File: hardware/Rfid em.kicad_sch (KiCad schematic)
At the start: 21 parts, among them IC1 EM4095, J1 Conn_01x06, U1 560uH, U2 AMS1117-5.0

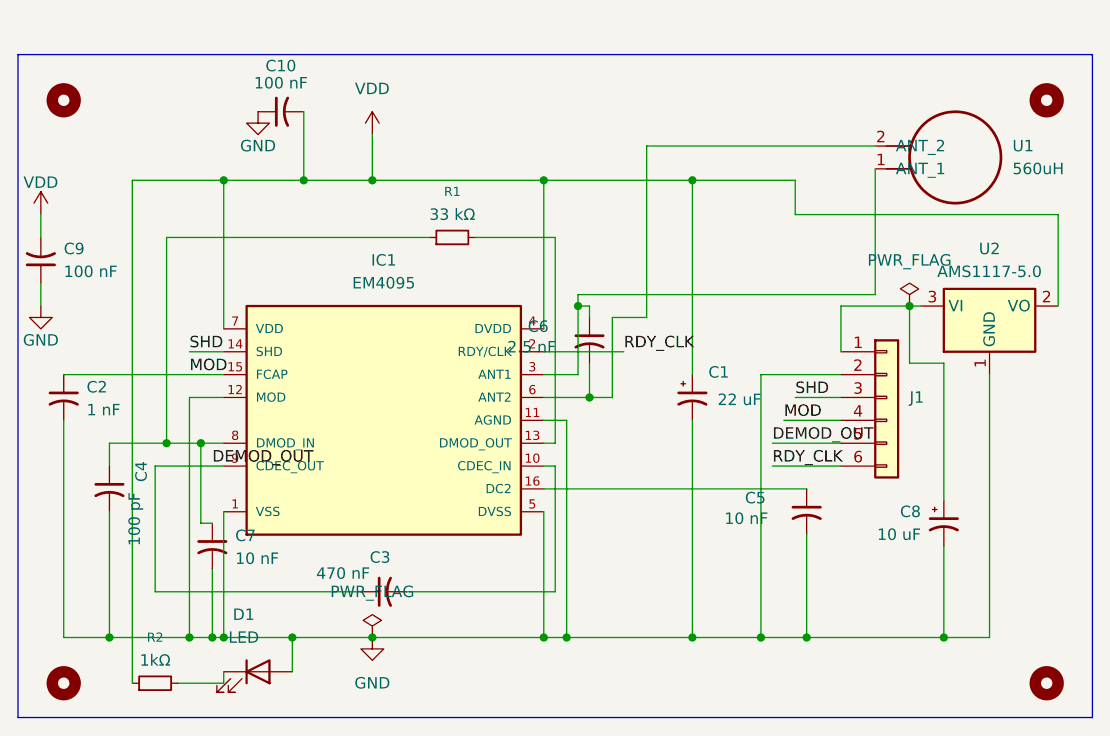
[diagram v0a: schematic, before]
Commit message: fix: Wire EM4095 per datasheet Fig. 8 and tune antenna to 134.2 kHz
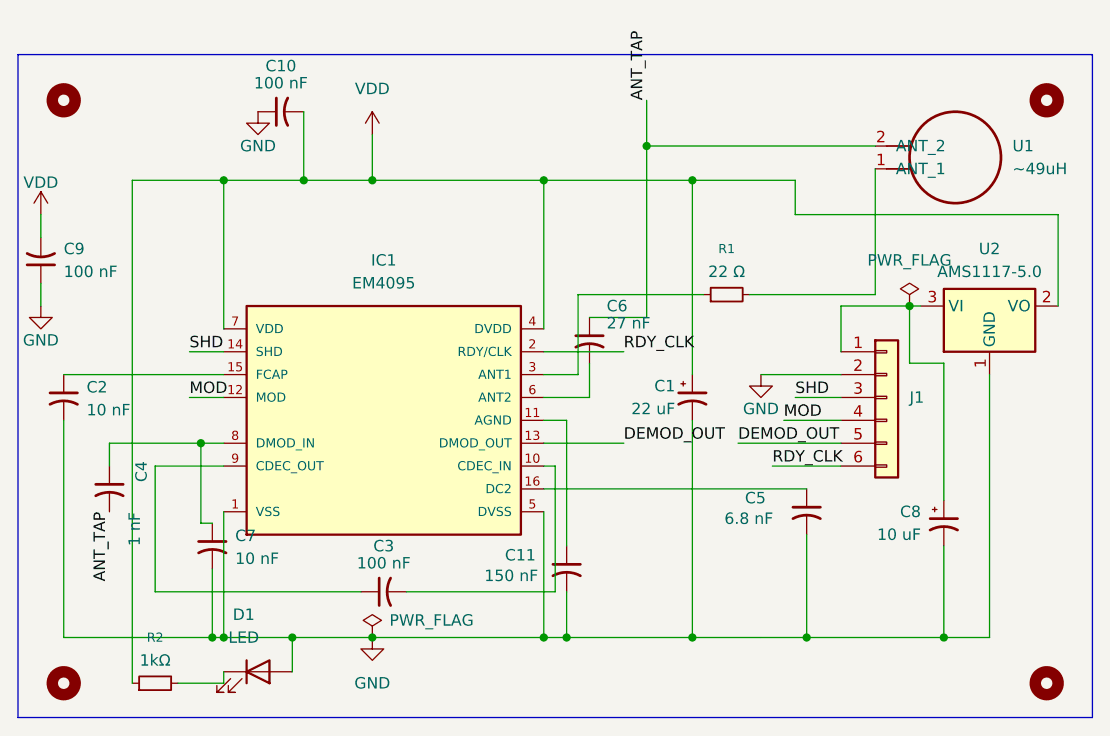
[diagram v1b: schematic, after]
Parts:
- added C11: 150 nF, Capacitor_SMD:C_0805_2012Metric, symbol Device:C_Small_US
- C2: value 1 nF -> 10 nF; Buying Links 1nF 102 0805 (2012 metric) 50V X7R MLCC SMD [4035] : Sunrom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 -> (none); MPN (none) -> C0805C103K5RACTU; Manufacturer (none) -> KEMET
- C3: value 470 nF -> 100 nF; Buying Links 470nF 474 0805 (2012 metric) 50V X7R MLCC SMD [3944] : Sunr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 -> (none); MPN (none) -> GRM21BR71H104KA01L; Manufacturer (none) -> Murata
- C4: value 100 pF -> 1 nF; Buying Links 100pF 101 0805 (2012 metric) 50V X7R MLCC SMD [4479] : Sunr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 -> (none); MPN (none) -> GRM2195C1H102JA01D; Manufacturer (none) -> Murata
- C5: value 10 nF -> 6.8 nF; Buying Links 10nF 103 0805 (2012 metric) 50V X7R MLCC SMD [4034] : Sunro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 -> (none); MPN (none) -> C0805C682K5RACTU; Manufacturer (none) -> KEMET
- C6: value 2.5 nF -> 27 nF; Buying Links 08055C242KAT2A KYOCERA AVX | Mouser India -> https://www.digikey.com/en/products/detail/murata-electroni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; MPN (none) -> GRM2165C1H273JA01D; Manufacturer (none) -> Murata
- C7: Buying Links 10nF 103 0805 (2012 metric) 50V X7R MLCC SMD [4034] : Sunro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 -> https://www.digikey.com/en/products/detail/murata-electroni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; MPN (none) -> GRM2195C1H103JA01D; Manufacturer (none) -> Murata
- D1: Buying Links Buy 1206 Surface mount LED White Online at Best Price | Rob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 -> (none); MPN (none) -> 158301250; Manufacturer (none) -> Würth Elektronik
- IC1: MPN (none) -> EM4095HMSO16B; Manufacturer (none) -> EM Microelectronic
- J1: Buying Links Buy Header Pins 40x1 - 2.54mm Pitch - Brass - KTRON India -> (none); MPN (none) -> 61300611121; Manufacturer (none) -> Würth Elektronik
- R1: value 33 kΩ -> 22 Ω; footprint Resistor_SMD:R_0805_2012Metric -> Resistor_SMD:R_2512_6332Metric; Buying Links 33K 1% 0805 [4321] : Sunrom Electronics -> https://www.digikey.com/en/products/detail/yageo/RC2512FK-0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; MPN (none) -> RC2512FK-0722RL; Manufacturer (none) -> Yageo
- R2: Buying Links Buy RT1206FRE071KL Resistors Online in India | Robu.in -> (none); MPN (none) -> CRCW12061K00FKEA; Manufacturer (none) -> Vishay
- U1: value 560uH -> ~49uH
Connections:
- net DEMOD_OUT: now also IC1.13 (DMOD_OUT); no longer C3.1, IC1.9 (CDEC_OUT)
- net GND: now also C11.2; no longer C4.2, IC1.11 (AGND), IC1.12 (MOD)
- net MOD: now also IC1.12 (MOD); no longer C2.1, IC1.15 (FCAP)
- net at C4.1, C7.1, IC1.8 (DMOD_IN): no longer R1.1
- net at R1.2: now also U1.1 (ANT_1); no longer IC1.13 (DMOD_OUT)
- net at C6.2, IC1.6 (ANT2): no longer U1.2 (ANT_2)
- new net: C11.1, IC1.11 (AGND)
- new net: C2.1, IC1.15 (FCAP)
- new net: IC1.3 (ANT1), R1.1
- new net: C3.1, IC1.9 (CDEC_OUT)
- new net ANT_TAP: C4.2, C6.1, U1.2 (ANT_2)
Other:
- moved on the sheet: R1
